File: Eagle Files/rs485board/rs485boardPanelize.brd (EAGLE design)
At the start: 63.5 x 76.7 mm, 95 parts, among them IC1 XC6206P332MR, IC2 MP2562, J1 AVR_SPI_PROG_3X2PTH, J2 RA 6Pin SMD, Q1 CJ3404, Q2 CJ3404, Q3 CJ3404, U1 ATMEGA328P_TQFP, U2 LIS3DH, U3 SP485, X1 RJ45-8P8C-8L-B, X3 RJ45-8P8C-8L-B, Y1 16MHz

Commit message: ready to panelize
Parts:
- added E$1: (no value), misc:MRK_DELTAX
- added E$2: (no value), misc:MRK_DELTAY
- added E$3: (no value), misc:MRK_DOWN_LEFT
- added E$4: 1, misc:NBR_MODX
- added E$5: 2, misc:NBR_MODY
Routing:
- removed copper zone on layer 1, net +5V
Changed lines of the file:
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@@
 <?xml version="1.0" encoding="utf-8"?>
 <!DOCTYPE eagle SYSTEM "eagle.dtd">
-<eagle version="8.7.0">
+<eagle version="9.0.0">
 <drawing>
 <settings>
@@
 <attribute name="VALUE" x="36.56" y="63.114" size="0.8128" layer="27" rot="R180"/>
 </element>
+<element name="E$1" library="misc" package="MRK_DELTAX" value="" x="71.12" y="-2.286"/>
+<element name="E$2" library="misc" package="MRK_DELTAY" value="" x="-6.604" y="76.454"/>
+<element name="E$3" library="misc" package="MRK_DOWN_LEFT" value="" x="-6.35" y="-3.81"/>
+<element name="E$4" library="misc" package="NBR_MODX" value="1" x="26.162" y="-5.08"/>
+<element name="E$5" library="misc" package="NBR_MODY" value="2" x="-21.844" y="42.418"/>
 </elements>
 <signals>
@@
 <contactref element="C38" pad="1"/>
 <contactref element="R9" pad="2"/>
-<polygon width="0.254" layer="1">
-<vertex x="36.068" y="56.642"/>
-<vertex x="37.338" y="56.642"/>
-<vertex x="37.592" y="56.896"/>
-<vertex x="38.354" y="57.658"/>
-<vertex x="38.354" y="72.644"/>
-<vertex x="38.354" y="74.676"/>
-<vertex x="38.1" y="74.93"/>
-<vertex x="36.83" y="74.93"/>
-<vertex x="36.576" y="74.676"/>
-<vertex x="36.068" y="74.168"/>
-</polygon>
-<wire x1="37.465" y1="69.85" x2="37.465" y2="62.119" width="1.27" layer="1"/>
-<wire x1="37.465" y1="62.119" x2="36.56" y2="61.214" width="0.254" layer="1"/>
-<wire x1="36.56" y1="61.214" x2="36.56" y2="57.404" width="0.254" layer="1"/>
+<wire x1="37.465" y1="69.85" x2="37.465" y2="62.119" width="1.524" layer="1"/>
+<wire x1="37.465" y1="62.119" x2="36.56" y2="61.214" width="0.762" layer="1"/>
+<wire x1="36.56" y1="61.214" x2="36.56" y2="57.404" width="0.762" layer="1"/>
 <via x="37.846" y="61.214" extent="1-16" drill="0.35"/>
 <via x="39.37" y="73.406" extent="1-16" drill="0.35"/>
@@
 <via x="9.906" y="69.85" extent="1-16" drill="0.35"/>
 <wire x1="9.906" y1="69.85" x2="9.906" y2="68.006" width="0.254" layer="1"/>
-<wire x1="36.56" y1="61.214" x2="37.846" y2="61.214" width="0.254" layer="1"/>
+<wire x1="36.56" y1="61.214" x2="37.846" y2="61.214" width="0.508" layer="1"/>
 <wire x1="37.846" y1="61.214" x2="38.862" y2="61.214" width="0.254" layer="1"/>
 <wire x1="38.862" y1="61.214" x2="39.37" y2="61.722" width="0.254" layer="1"/>

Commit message: adjust spacing
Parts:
- E$4: value 1 -> 2
- moved E$1 8.01 mm to (63.1, -2.54)
- moved E$2 4.06 mm to (-2.54, 76.5)
- moved E$3 4.02 mm to (-2.54, -2.54)
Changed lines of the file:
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@@
 <attribute name="VALUE" x="36.56" y="63.114" size="0.8128" layer="27" rot="R180"/>
 </element>
-<element name="E$1" library="misc" package="MRK_DELTAX" value="" x="71.12" y="-2.286"/>
-<element name="E$2" library="misc" package="MRK_DELTAY" value="" x="-6.604" y="76.454"/>
-<element name="E$3" library="misc" package="MRK_DOWN_LEFT" value="" x="-6.35" y="-3.81"/>
-<element name="E$4" library="misc" package="NBR_MODX" value="1" x="26.162" y="-5.08"/>
+<element name="E$1" library="misc" package="MRK_DELTAX" value="" x="63.119" y="-2.54"/>
+<element name="E$2" library="misc" package="MRK_DELTAY" value="" x="-2.54" y="76.454"/>
+<element name="E$3" library="misc" package="MRK_DOWN_LEFT" value="" x="-2.54" y="-2.54"/>
+<element name="E$4" library="misc" package="NBR_MODX" value="2" x="26.162" y="-5.08"/>
 <element name="E$5" library="misc" package="NBR_MODY" value="2" x="-21.844" y="42.418"/>
 </elements>

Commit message: clean up 2*2
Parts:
- added C10X12, C10X21, C10X22, C14X12, C14X21, C14X22, C15X12, C15X21, C15X22, C16X12, C16X21, C16X22, C17X12, C17X21, C17X22, C18X12, C18X21, C18X22, C19X12, C19X21, C19X22, C1X12, C1X21, C1X22, C20X12, C20X21, C20X22, C21X12, C21X21, C21X22, C22X12, C22X21, C22X22, C23X12, C23X21, C23X22, C24X12, C24X21, C24X22, C25X12, C25X21, C25X22, C26X12, C26X21, C26X22, C3X12, C3X21, C3X22, C4X12, C4X21, C4X22, C5X12, C5X21, C5X22, C7X12, C7X21, C7X22, C8X12, C8X21, C8X22, C9X12, C9X21, C9X22: 0.1uF, resistor:C0805K
- added C12X12, C12X21, C12X22, C2X12, C2X21, C2X22, C38X12, C38X21, C38X22, C6X12, C6X21, C6X22: 10uF, resistor:C0805K
- added C13X12, C13X21, C13X22, C27X12, C27X21, C27X22, C28X12, C28X21, C28X22, C29X12, C29X21, C29X22, C30X12, C30X21, C30X22, C31X12, C31X21, C31X22, C32X12, C32X21, C32X22, C33X12, C33X21, C33X22, C34X12, C34X21, C34X22, C35X12, C35X21, C35X22: 1uF 100V, SparkFun-Capacitors:1206
- added C36X12, C36X21, C36X22: 150pF, resistor:C0805K
- added D10X12, D10X21, D10X22, D11X12, D11X21, D11X22, D12X12, D12X21, D12X22, D13X12, D13X21, D13X22, D14X12, D14X21, D14X22, D15X12, D15X21, D15X22, D16X12, D16X21, D16X22, D17X12, D17X21, D17X22, D18X12, D18X21, D18X22, D7X12, D7X21, D7X22, D8X12, D8X21, D8X22, D9X12, D9X21, D9X22: WS2812B, SparkFun-LED:WS2812B
- added D1X12, D1X21, D1X22, D2X12, D2X21, D2X22, D3X12, D3X21, D3X22, D4X12, D4X21, D4X22, D5X12, D5X21, D5X22, D6X12, D6X21, D6X22: 5819, adafruit:SOD-123
- added D20X12, D20X21, D20X22: B280-13-F, diode:DO214AA
- added IC1X12, IC1X21, IC1X22: XC6206P332MR, linear:SOT23
- added IC2X12, IC2X21, IC2X22: MP2562, misc:SO08
- added J1X12, J1X21, J1X22: AVR_SPI_PROG_3X2PTH, SparkFun-Connectors:2X3
- added J2X12, J2X21, J2X22: RA 6Pin SMD, SparkFun-Connectors:1X06-SMD_RA_MALE
- added J3X12, J3X21, J3X22, J4X12, J4X21, J4X22, J5X12, J5X21, J5X22, J6X12, J6X21, J6X22: (no value), SparkFun-Connectors:1X01
- added L1X12, L1X21, L1X22: 15uH, misc:SLF12575
- added PAD1X12, PAD1X21, PAD1X22, PAD2X12, PAD2X21, PAD2X22, PAD3X12, PAD3X21, PAD3X22, PAD4X12, PAD4X21, PAD4X22, PAD5X12, PAD5X21, PAD5X22: (no value), wirepad:1,6/0,8
- added Q1X12, Q1X21, Q1X22, Q2X12, Q2X21, Q2X22, Q3X12, Q3X21, Q3X22: CJ3404, SparkFun-DiscreteSemi:SOT23-3
- added R10X12, R10X21, R10X22: 40.2k, resistor:R0805
- added R11X12, R11X21, R11X22: 120, resistor:R0805
- added R12X12, R12X21, R12X22, R13X12, R13X21, R13X22: 1K, resistor:R0805
- added R14X12, R14X21, R14X22, R1X12, R1X21, R1X22, R5X12, R5X21, R5X22, R6X12, R6X21, R6X22, R7X12, R7X21, R7X22: 10K, resistor:R0805
- added R15X12, R15X21, R15X22: 17.4K, resistor:R0805
- added R16X12, R16X21, R16X22: 200K, resistor:R0805
- added R17X12, R17X21, R17X22: 158K, resistor:R0805
- added R2X12, R2X21, R2X22, R3X12, R3X21, R3X22, R4X12, R4X21, R4X22: DNP, resistor:R0805
- added R8X12, R8X21, R8X22: 100K, resistor:R0805
- added R9X12, R9X21, R9X22: 210K, resistor:R0805
- added U1X12, U1X21, U1X22: ATMEGA328P_TQFP, SparkFun-IC-Microcontroller:TQFP32-08
- added U2X12, U2X21, U2X22: LIS3DH, SparkFun-Sensors:LGA-16-3X3
- added U3X12, U3X21, U3X22: SP485, SparkFun-IC-Comms:SO08
- added X1X12, X1X21, X1X22, X3X12, X3X21, X3X22: RJ45-8P8C-8L-B, myownParts:RJ45-SHIELD-DS1128-S80BP
- added Y1X12, Y1X21, Y1X22: 16MHz, SparkFun-Clocks:RESONATOR-SMD-3.2X1.3
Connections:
- new net +24VX12: C13X12.1, C27X12.1, C28X12.1, C29X12.1, C30X12.1, C31X12.1, C32X12.1, C33X12.1, C34X12.1, C35X12.1, IC2X12.7, R8X12.2, X1X12.4, X1X12.5, X3X12.4, X3X12.5
- new net +24VX21: C13X21.1, C27X21.1, C28X21.1, C29X21.1, C30X21.1, C31X21.1, C32X21.1, C33X21.1, C34X21.1, C35X21.1, IC2X21.7, R8X21.2, X1X21.4, X1X21.5, X3X21.4, X3X21.5
- new net +24VX22: C13X22.1, C27X22.1, C28X22.1, C29X22.1, C30X22.1, C31X22.1, C32X22.1, C33X22.1, C34X22.1, C35X22.1, IC2X22.7, R8X22.2, X1X22.4, X1X22.5, X3X22.4, X3X22.5
- new net +3V3X12: C6X12.1, C7X12.1, C9X12.1, IC1X12.2, R5X12.2, R6X12.2, R7X12.2, U2X12.1, U2X12.14
- new net +3V3X21: C6X21.1, C7X21.1, C9X21.1, IC1X21.2, R5X21.2, R6X21.2, R7X21.2, U2X21.1, U2X21.14
- new net +3V3X22: C6X22.1, C7X22.1, C9X22.1, IC1X22.2, R5X22.2, R6X22.2, R7X22.2, U2X22.1, U2X22.14
- new net +5VX12: C12X12.1, C14X12.1, C15X12.1, C16X12.1, C17X12.1, C18X12.1, C19X12.1, C20X12.1, C21X12.1, C22X12.1, C23X12.1, C24X12.1, C25X12.1, C26X12.1, C2X12.1, C38X12.1, C3X12.1, C4X12.1, C8X12.1, D10X12.1, D11X12.1, D12X12.1, D13X12.1, D14X12.1, D15X12.1, D16X12.1, D17X12.1, D18X12.1, D7X12.1, D8X12.1, D9X12.1, IC1X12.3, J1X12.2, J2X12.4, J6X12.1, L1X12.P$2, R14X12.2, R1X12.2, R9X12.2, U1X12.18, U1X12.4, U1X12.6, U3X12.8
- new net +5VX21: C12X21.1, C14X21.1, C15X21.1, C16X21.1, C17X21.1, C18X21.1, C19X21.1, C20X21.1, C21X21.1, C22X21.1, C23X21.1, C24X21.1, C25X21.1, C26X21.1, C2X21.1, C38X21.1, C3X21.1, C4X21.1, C8X21.1, D10X21.1, D11X21.1, D12X21.1, D13X21.1, D14X21.1, D15X21.1, D16X21.1, D17X21.1, D18X21.1, D7X21.1, D8X21.1, D9X21.1, IC1X21.3, J1X21.2, J2X21.4, J6X21.1, L1X21.P$2, R14X21.2, R1X21.2, R9X21.2, U1X21.18, U1X21.4, U1X21.6, U3X21.8
- new net +5VX22: C12X22.1, C14X22.1, C15X22.1, C16X22.1, C17X22.1, C18X22.1, C19X22.1, C20X22.1, C21X22.1, C22X22.1, C23X22.1, C24X22.1, C25X22.1, C26X22.1, C2X22.1, C38X22.1, C3X22.1, C4X22.1, C8X22.1, D10X22.1, D11X22.1, D12X22.1, D13X22.1, D14X22.1, D15X22.1, D16X22.1, D17X22.1, D18X22.1, D7X22.1, D8X22.1, D9X22.1, IC1X22.3, J1X22.2, J2X22.4, J6X22.1, L1X22.P$2, R14X22.2, R1X22.2, R9X22.2, U1X22.18, U1X22.4, U1X22.6, U3X22.8
- new net A3X12: D7X12.4, U1X12.26
- new net A3X21: D7X21.4, U1X21.26
- new net A3X22: D7X22.4, U1X22.26
- new net A4X12: PAD3X12.1, U1X12.27
- new net A4X21: PAD3X21.1, U1X21.27
- new net A4X22: PAD3X22.1, U1X22.27
- new net A5X12: PAD4X12.1, U1X12.28
- new net A5X21: PAD4X21.1, U1X21.28
- new net A5X22: PAD4X22.1, U1X22.28
- new net AREFX12: C5X12.2, U1X12.20
- new net AREFX21: C5X21.2, U1X21.20
- new net AREFX22: C5X22.2, U1X22.20
- new net BSTX12: C10X12.1, IC2X12.8
- new net BSTX21: C10X21.1, IC2X21.8
- new net BSTX22: C10X22.1, IC2X22.8
- new net COMPX12: C36X12.1, IC2X12.3
- new net COMPX21: C36X21.1, IC2X21.3
- new net COMPX22: C36X22.1, IC2X22.3
- new net D2X12: D5X12.C, U1X12.32
- new net D2X21: D5X21.C, U1X21.32
- new net D2X22: D5X22.C, U1X22.32
- new net D3X12: D6X12.C, U1X12.1
- new net D3X21: D6X21.C, U1X21.1
- new net D3X22: D6X22.C, U1X22.1
- new net D5X12: Q3X12.1, U1X12.9
- new net D5X21: Q3X21.1, U1X21.9
- new net D5X22: Q3X22.1, U1X22.9
- new net D6X12: Q2X12.1, U1X12.10
- new net D6X21: Q2X21.1, U1X21.10
- new net D6X22: Q2X22.1, U1X22.10
- new net D7X12: PAD1X12.1, U1X12.11
- new net D7X21: PAD1X21.1, U1X21.11
- new net D7X22: PAD1X22.1, U1X22.11
- new net D8X12: PAD2X12.1, U1X12.12
- new net D8X21: PAD2X21.1, U1X21.12
- new net D8X22: PAD2X22.1, U1X22.12
- new net D9X12: Q1X12.1, U1X12.13
- new net D9X21: Q1X21.1, U1X21.13
- new net D9X22: Q1X22.1, U1X22.13
- new net DIRX12: U1X12.2, U3X12.2, U3X12.3
- new net DIRX21: U1X21.2, U3X21.2, U3X21.3
- new net DIRX22: U1X22.2, U3X22.2, U3X22.3
- new net ENX12: IC2X12.2, R15X12.2, R8X12.1
- new net ENX21: IC2X21.2, R15X21.2, R8X21.1
- new net ENX22: IC2X22.2, R15X22.2, R8X22.1
- new net FBX12: IC2X12.4, R10X12.2, R9X12.1
- new net FBX21: IC2X21.4, R10X21.2, R9X21.1
- new net FBX22: IC2X22.4, R10X22.2, R9X22.1
- new net FREQX12: IC2X12.6, R16X12.2
- new net FREQX21: IC2X21.6, R16X21.2
- new net FREQX22: IC2X22.6, R16X22.2
- new net GNDX12: C12X12.2, C13X12.2, C14X12.2, C15X12.2, C16X12.2, C17X12.2, C18X12.2, C19X12.2, C20X12.2, C21X12.2, C22X12.2, C23X12.2, C24X12.2, C25X12.2, C26X12.2, C27X12.2, C28X12.2, C29X12.2, C2X12.2, C30X12.2, C31X12.2, C32X12.2, C33X12.2, C34X12.2, C35X12.2, C38X12.2, C3X12.2, C4X12.2, C5X12.1, C6X12.2, C7X12.2, C8X12.2, C9X12.2, D10X12.3, D11X12.3, D12X12.3, D13X12.3, D14X12.3, D15X12.3, D16X12.3, D17X12.3, D18X12.3, D20X12.A, D7X12.3, D8X12.3, D9X12.3, IC1X12.1, IC2X12.5, J1X12.6, J2X12.6, PAD5X12.1, Q1X12.2, Q2X12.2, Q3X12.2, R10X12.1, R15X12.1, R16X12.1, R17X12.1, U1X12.21, U1X12.3, U1X12.5, U2X12.10, U2X12.12, U2X12.5, U3X12.5, X1X12.3, X1X12.6, X1X12.7, X1X12.8, X3X12.3, X3X12.6, X3X12.7, X3X12.8, Y1X12.2
- new net GNDX21: C12X21.2, C13X21.2, C14X21.2, C15X21.2, C16X21.2, C17X21.2, C18X21.2, C19X21.2, C20X21.2, C21X21.2, C22X21.2, C23X21.2, C24X21.2, C25X21.2, C26X21.2, C27X21.2, C28X21.2, C29X21.2, C2X21.2, C30X21.2, C31X21.2, C32X21.2, C33X21.2, C34X21.2, C35X21.2, C38X21.2, C3X21.2, C4X21.2, C5X21.1, C6X21.2, C7X21.2, C8X21.2, C9X21.2, D10X21.3, D11X21.3, D12X21.3, D13X21.3, D14X21.3, D15X21.3, D16X21.3, D17X21.3, D18X21.3, D20X21.A, D7X21.3, D8X21.3, D9X21.3, IC1X21.1, IC2X21.5, J1X21.6, J2X21.6, PAD5X21.1, Q1X21.2, Q2X21.2, Q3X21.2, R10X21.1, R15X21.1, R16X21.1, R17X21.1, U1X21.21, U1X21.3, U1X21.5, U2X21.10, U2X21.12, U2X21.5, U3X21.5, X1X21.3, X1X21.6, X1X21.7, X1X21.8, X3X21.3, X3X21.6, X3X21.7, X3X21.8, Y1X21.2
- new net GNDX22: C12X22.2, C13X22.2, C14X22.2, C15X22.2, C16X22.2, C17X22.2, C18X22.2, C19X22.2, C20X22.2, C21X22.2, C22X22.2, C23X22.2, C24X22.2, C25X22.2, C26X22.2, C27X22.2, C28X22.2, C29X22.2, C2X22.2, C30X22.2, C31X22.2, C32X22.2, C33X22.2, C34X22.2, C35X22.2, C38X22.2, C3X22.2, C4X22.2, C5X22.1, C6X22.2, C7X22.2, C8X22.2, C9X22.2, D10X22.3, D11X22.3, D12X22.3, D13X22.3, D14X22.3, D15X22.3, D16X22.3, D17X22.3, D18X22.3, D20X22.A, D7X22.3, D8X22.3, D9X22.3, IC1X22.1, IC2X22.5, J1X22.6, J2X22.6, PAD5X22.1, Q1X22.2, Q2X22.2, Q3X22.2, R10X22.1, R15X22.1, R16X22.1, R17X22.1, U1X22.21, U1X22.3, U1X22.5, U2X22.10, U2X22.12, U2X22.5, U3X22.5, X1X22.3, X1X22.6, X1X22.7, X1X22.8, X3X22.3, X3X22.6, X3X22.7, X3X22.8, Y1X22.2
- new net INT1X12: D5X12.A, U2X12.11
- new net INT1X21: D5X21.A, U2X21.11
- new net INT1X22: D5X22.A, U2X22.11
- new net INT2X12: D6X12.A, U2X12.9
- new net INT2X21: D6X21.A, U2X21.9
- new net INT2X22: D6X22.A, U2X22.9
- new net MISOX12: D3X12.C, J1X12.1, U1X12.16
- new net MISOX21: D3X21.C, J1X21.1, U1X21.16
- new net MISOX22: D3X22.C, J1X22.1, U1X22.16
- new net MISO_3.3VX12: D3X12.A, U2X12.7
- new net MISO_3.3VX21: D3X21.A, U2X21.7
- new net MISO_3.3VX22: D3X22.A, U2X22.7
- new net MOSIX12: D2X12.C, J1X12.4, U1X12.15
- new net MOSIX21: D2X21.C, J1X21.4, U1X21.15
- new net MOSIX22: D2X22.C, J1X22.4, U1X22.15
- new net MOSI_3.3VX12: D2X12.A, R6X12.1, U2X12.6
- new net MOSI_3.3VX21: D2X21.A, R6X21.1, U2X21.6
- new net MOSI_3.3VX22: D2X22.A, R6X22.1, U2X22.6
- new net N$10X12: D10X12.2, D11X12.4
- new net N$10X21: D10X21.2, D11X21.4
- new net N$10X22: D10X22.2, D11X22.4
- new net N$11X12: D11X12.2, D12X12.4
- new net N$11X21: D11X21.2, D12X21.4
- new net N$11X22: D11X22.2, D12X22.4
- new net N$12X12: D12X12.2, D13X12.4
- new net N$12X21: D12X21.2, D13X21.4
- new net N$12X22: D12X22.2, D13X22.4
- new net N$13X12: D13X12.2, D14X12.4
- new net N$13X21: D13X21.2, D14X21.4
- new net N$13X22: D13X22.2, D14X22.4
- new net N$14X12: D14X12.2, D15X12.4
- new net N$14X21: D14X21.2, D15X21.4
- new net N$14X22: D14X22.2, D15X22.4
- new net N$15X12: D15X12.2, D16X12.4
- new net N$15X21: D15X21.2, D16X21.4
- new net N$15X22: D15X22.2, D16X22.4
- new net N$16X12: D16X12.2, D17X12.4
- new net N$16X21: D16X21.2, D17X21.4
- new net N$16X22: D16X22.2, D17X22.4
- new net N$17X12: D17X12.2, D18X12.4
- new net N$17X21: D17X21.2, D18X21.4
- new net N$17X22: D17X22.2, D18X22.4
- new net N$1X12: Q1X12.3, R2X12.1
- new net N$1X21: Q1X21.3, R2X21.1
- new net N$1X22: Q1X22.3, R2X22.1
- new net N$25X12: C36X12.2, R17X12.2
- new net N$25X21: C36X21.2, R17X21.2
- new net N$25X22: C36X22.2, R17X22.2
- new net N$2X12: D7X12.2, D8X12.4
- new net N$2X21: D7X21.2, D8X21.4
- new net N$2X22: D7X22.2, D8X22.4
- new net N$30X12: R12X12.2, U3X12.1
- new net N$30X21: R12X21.2, U3X21.1
- new net N$30X22: R12X22.2, U3X22.1
- new net N$31X12: R13X12.2, U3X12.4
- new net N$31X21: R13X21.2, U3X21.4
- new net N$31X22: R13X22.2, U3X22.4
- new net N$3X12: D8X12.2, D9X12.4
- new net N$3X21: D8X21.2, D9X21.4
- new net N$3X22: D8X22.2, D9X22.4
- new net N$4X12: J3X12.1, R2X12.2
- new net N$4X21: J3X21.1, R2X21.2
- new net N$4X22: J3X22.1, R2X22.2
- new net N$5X12: Q2X12.3, R3X12.1
- new net N$5X21: Q2X21.3, R3X21.1
- new net N$5X22: Q2X22.3, R3X22.1
- new net N$6X12: J4X12.1, R3X12.2
- new net N$6X21: J4X21.1, R3X21.2
- new net N$6X22: J4X22.1, R3X22.2
- new net N$7X12: Q3X12.3, R4X12.1
- new net N$7X21: Q3X21.3, R4X21.1
- new net N$7X22: Q3X22.3, R4X22.1
- new net N$8X12: J5X12.1, R4X12.2
- new net N$8X21: J5X21.1, R4X21.2
- new net N$8X22: J5X22.1, R4X22.2
- new net N$9X12: D10X12.4, D9X12.2
- new net N$9X21: D10X21.4, D9X21.2
- new net N$9X22: D10X22.4, D9X22.2
- new net RESETX12: C1X12.2, J1X12.5, R1X12.1, U1X12.29
- new net RESETX21: C1X21.2, J1X21.5, R1X21.1, U1X21.29
- new net RESETX22: C1X22.2, J1X22.5, R1X22.1, U1X22.29
- new net RESET_EXTX12: C1X12.1, J2X12.1
- new net RESET_EXTX21: C1X21.1, J2X21.1
- new net RESET_EXTX22: C1X22.1, J2X22.1
- new net RS485AX12: R11X12.1, U3X12.6, X1X12.2, X3X12.2
- new net RS485AX21: R11X21.1, U3X21.6, X1X21.2, X3X21.2
- new net RS485AX22: R11X22.1, U3X22.6, X1X22.2, X3X22.2
- new net RS485BX12: R11X12.2, U3X12.7, X1X12.1, X3X12.1
- new net RS485BX21: R11X21.2, U3X21.7, X1X21.1, X3X21.1
- new net RS485BX22: R11X22.2, U3X22.7, X1X22.1, X3X22.1
- new net RXX12: J2X12.3, R12X12.1, R14X12.1, U1X12.30
- new net RXX21: J2X21.3, R12X21.1, R14X21.1, U1X21.30
- new net RXX22: J2X22.3, R12X22.1, R14X22.1, U1X22.30
- new net SCKX12: D4X12.C, J1X12.3, U1X12.17
- new net SCKX21: D4X21.C, J1X21.3, U1X21.17
- new net SCKX22: D4X22.C, J1X22.3, U1X22.17
- new net SCK_3.3VX12: D4X12.A, R7X12.1, U2X12.4
- new net SCK_3.3VX21: D4X21.A, R7X21.1, U2X21.4
- new net SCK_3.3VX22: D4X22.A, R7X22.1, U2X22.4
- new net SSX12: D1X12.C, U1X12.14
- new net SSX21: D1X21.C, U1X21.14
- new net SSX22: D1X22.C, U1X22.14
- new net SS_3.3VX12: D1X12.A, R5X12.1, U2X12.8
- new net SS_3.3VX21: D1X21.A, R5X21.1, U2X21.8
- new net SS_3.3VX22: D1X22.A, R5X22.1, U2X22.8
- new net SWX12: C10X12.2, D20X12.C, IC2X12.1, L1X12.P$1
- new net SWX21: C10X21.2, D20X21.C, IC2X21.1, L1X21.P$1
- new net SWX22: C10X22.2, D20X22.C, IC2X22.1, L1X22.P$1
- new net TXX12: J2X12.2, R13X12.1, U1X12.31
- new net TXX21: J2X21.2, R13X21.1, U1X21.31
- new net TXX22: J2X22.2, R13X22.1, U1X22.31
- new net XTAL1X12: U1X12.7, Y1X12.1
- new net XTAL1X21: U1X21.7, Y1X21.1
- new net XTAL1X22: U1X22.7, Y1X22.1
- new net XTAL2X12: U1X12.8, Y1X12.3
- new net XTAL2X21: U1X21.8, Y1X21.3
- new net XTAL2X22: U1X22.8, Y1X22.3
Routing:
- net GNDX22: track 0.00 -> 654.9 mm, vias 0 -> 70
- net GNDX21: track 0.00 -> 654.9 mm, vias 0 -> 70
- net GNDX12: track 0.00 -> 654.9 mm, vias 0 -> 70
- net +5VX21: track 0.00 -> 417.0 mm, vias 0 -> 14
- net +5VX22: track 0.00 -> 417.0 mm, vias 0 -> 14
- net +5VX12: track 0.00 -> 417.0 mm, vias 0 -> 14
- net +24VX22: track 0.00 -> 119.4 mm, vias 0 -> 2
- net +24VX12: track 0.00 -> 119.4 mm, vias 0 -> 2
- net +24VX21: track 0.00 -> 119.4 mm, vias 0 -> 2
- net RS485AX21: track 0.00 -> 88.7 mm
- net RS485AX22: track 0.00 -> 88.7 mm
- net RS485AX12: track 0.00 -> 88.7 mm
- net TXX22: track 0.00 -> 75.9 mm, vias 0 -> 2
- net TXX21: track 0.00 -> 75.9 mm, vias 0 -> 2
- net TXX12: track 0.00 -> 75.9 mm, vias 0 -> 2
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- added copper zone on layer 1, net GNDX12
- added copper zone on layer 16, net GNDX12
- added copper zone on layer 1, net GNDX21
- added copper zone on layer 16, net GNDX21
- added copper zone on layer 1, net GNDX22
- added copper zone on layer 16, net GNDX22
- added copper zone on layer 1, net SWX12
- added copper zone on layer 1, net SWX21
- added copper zone on layer 1, net SWX22
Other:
- board size 63.5 x 76.7 mm -> 129.2 x 155.6 mm
- board text added: "C14"
- board text added: "C15"
- board text added: "C16"
- board text added: "C17"
- board text added: "C18"
- board text added: "C19"
- board text added: "C20"
- board text added: "C21"
- board text added: "C22"
- board text added: "C23"
- board text added: "C24"
- board text added: "C25"
- board text added: "C32"
- board text added: "D10"
- board text added: "D11"
- board text added: "D12"
- board text added: "D13"
- board text added: "D14"
- board text added: "D15"
- board text added: "D16"
- board text added: "D17"
- board text added: "D18"
- board text added: "D7"
- board text added: "D8"
- board text added: "D9"
- board text added: "J2"
- board text added: "Think Create LLC'"

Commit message: move to AB 2*2
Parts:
- removed E$1: (no value), misc:MRK_DELTAX
- removed E$2: (no value), misc:MRK_DELTAY
- removed E$3: (no value), misc:MRK_DOWN_LEFT
- removed E$4: 2, misc:NBR_MODX
- removed E$5: 2, misc:NBR_MODY
- moved PAD1 141.0 mm to (127.6, 70.0), turned to 180 degrees
- moved PAD2 139.5 mm to (126.1, 71.2), turned to 180 degrees
- moved Y1 135.1 mm to (126.6, 65.2), turned to 90 degrees
- moved C3 130.6 mm to (125.6, 61.6), turned to 0 degrees
- moved C4 129.0 mm to (125.6, 59.3), turned to 0 degrees
- moved D4 128.4 mm to (127.1, 53.0), turned to 270 degrees
- moved R16 127.1 mm to (122.3, 11.8), turned to 270 degrees
- moved R7 126.4 mm to (127.1, 47.6), turned to 270 degrees
- moved J2X21 126.1 mm to (8.89, 67.9), turned to 270 degrees
- moved C32X21 124.6 mm to (9.40, 9.53), turned to 0 degrees
- moved D2 124.5 mm to (125.1, 53.0), turned to 270 degrees
- moved R13X21 124.2 mm to (3.81, 51.2), turned to 270 degrees
- moved R9 123.4 mm to (119.3, 9.78), turned to 270 degrees
- moved U1 122.6 mm to (119.0, 66.7), turned to 135 degrees
- moved C8 122.3 mm to (125.6, 42.5), turned to 90 degrees
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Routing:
- net D6: track 43.1 -> 42.1 mm
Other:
- board size 129.2 x 155.6 mm -> 129.2 x 155.5 mm

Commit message: panel finish, need add fiducial
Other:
- board size 129.2 x 155.5 mm -> 139.6 x 155.8 mm

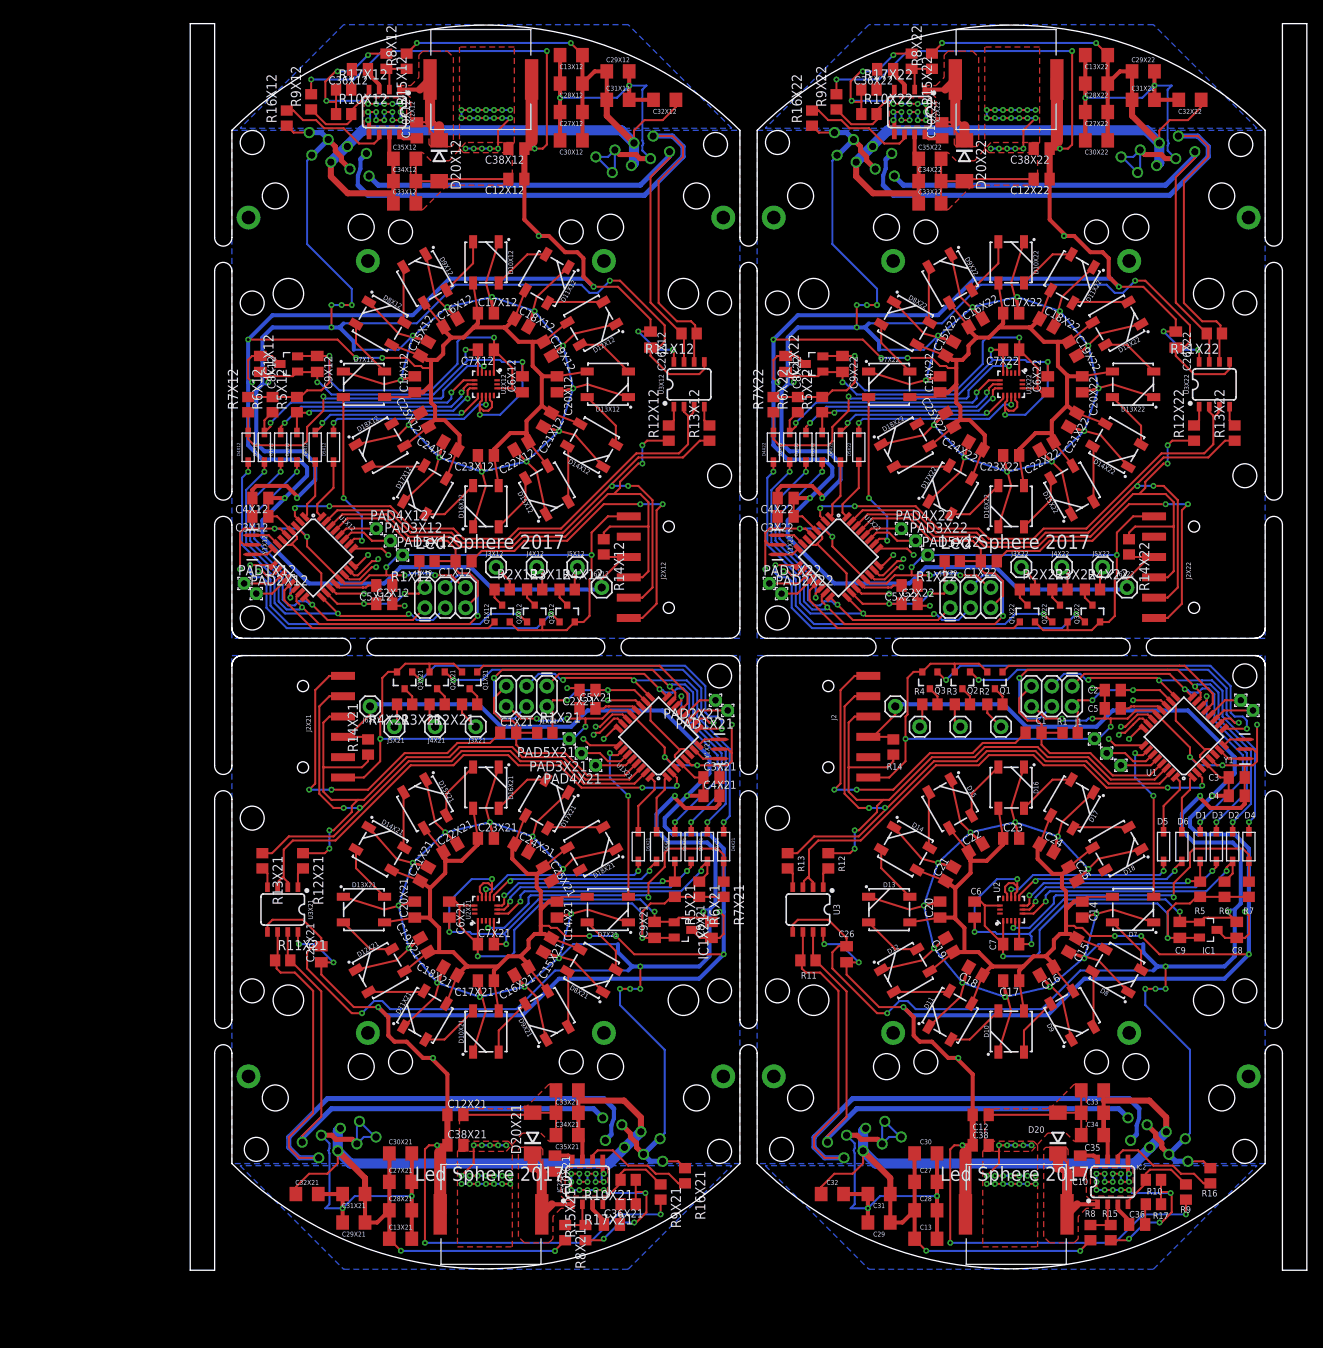
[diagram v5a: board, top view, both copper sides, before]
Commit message: add fiducial
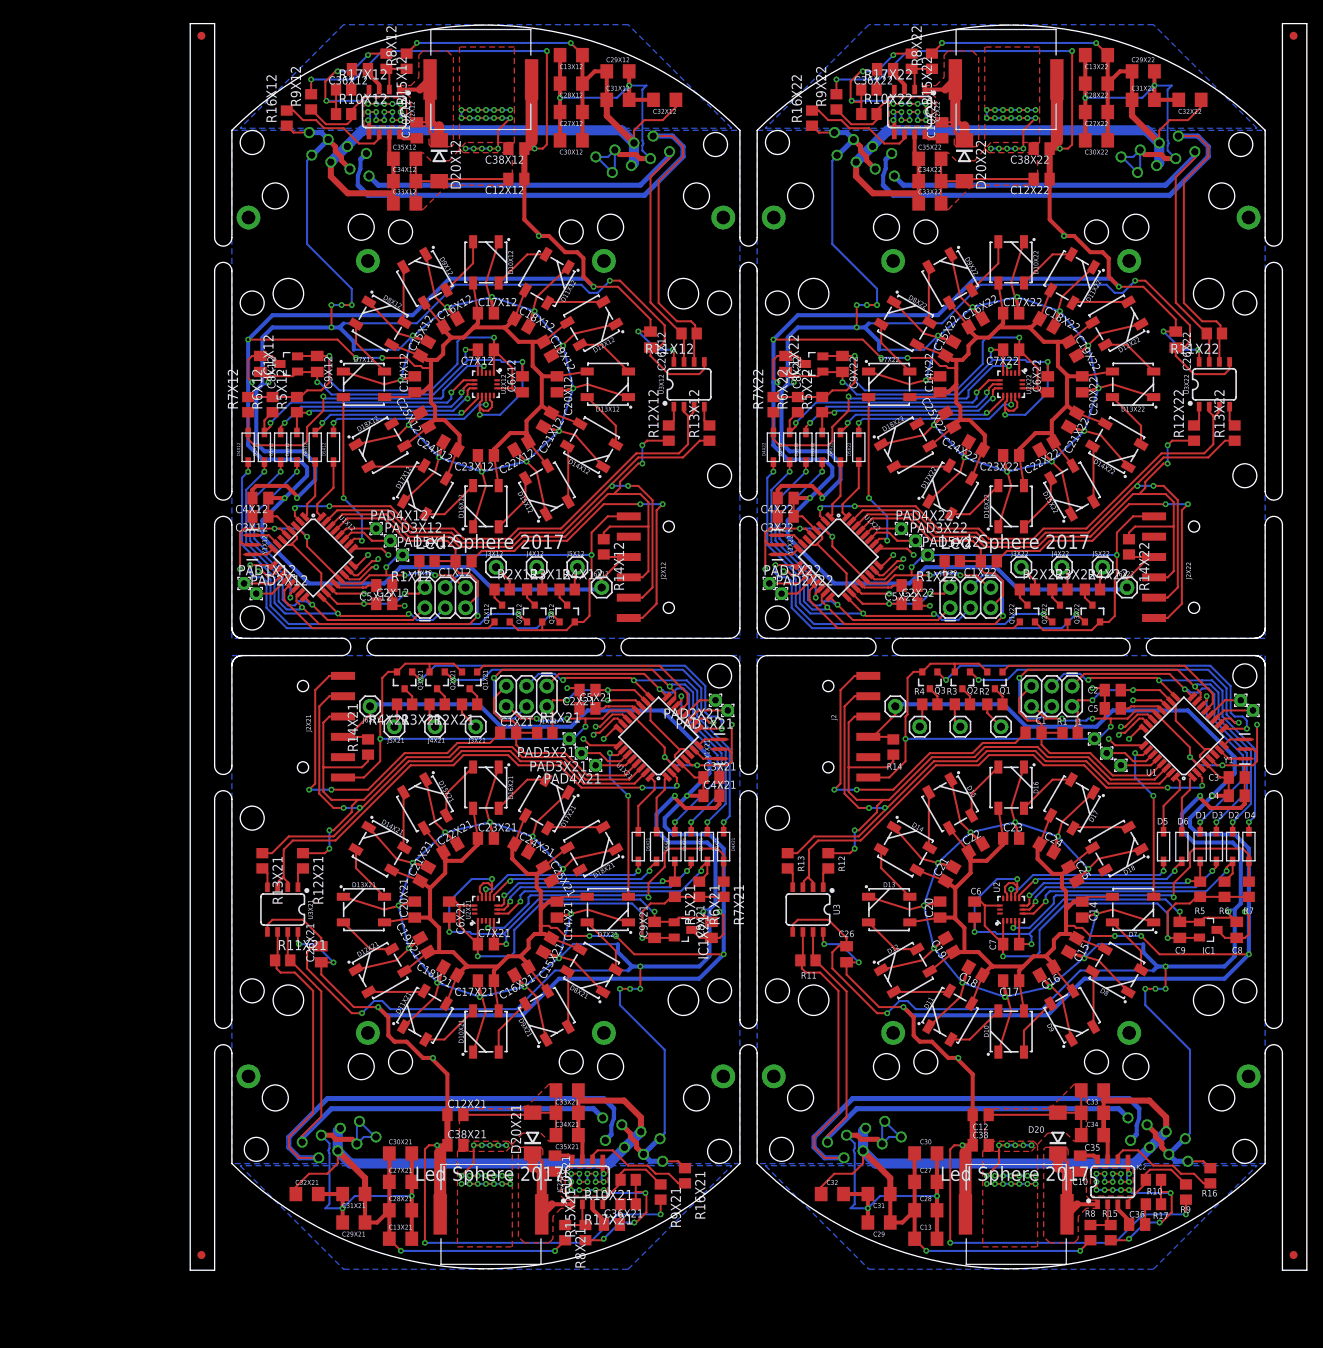
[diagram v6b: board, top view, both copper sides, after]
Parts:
- added E$1, E$2, E$3, E$4: (no value), SparkFun-Aesthetics:FIDUCIAL-1X2
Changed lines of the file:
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@@
 <element name="X3X22" library="myownParts" package="RJ45-SHIELD-DS1128-S80BP" value="RJ45-8P8C-8L-B" x="76.454" y="132.334" rot="MR20"/>
 <element name="Y1X22" library="SparkFun-Clocks" library_urn="urn:adsk.eagle:library:511" package="RESONATOR-SMD-3.2X1.3" package3d_urn="urn:adsk.eagle:package:37551/1" value="16MHz" x="68.199" y="90.678" rot="R270"/>
+<element name="E$1" library="SparkFun-Aesthetics" library_urn="urn:adsk.eagle:library:507" package="FIDUCIAL-1X2" package3d_urn="urn:adsk.eagle:package:37108/1" value="" x="-3.81" y="154.305"/>
+<element name="E$2" library="SparkFun-Aesthetics" library_urn="urn:adsk.eagle:library:507" package="FIDUCIAL-1X2" package3d_urn="urn:adsk.eagle:package:37108/1" value="" x="-3.81" y="1.905"/>
+<element name="E$3" library="SparkFun-Aesthetics" library_urn="urn:adsk.eagle:library:507" package="FIDUCIAL-1X2" package3d_urn="urn:adsk.eagle:package:37108/1" value="" x="132.715" y="1.905"/>
+<element name="E$4" library="SparkFun-Aesthetics" library_urn="urn:adsk.eagle:library:507" package="FIDUCIAL-1X2" package3d_urn="urn:adsk.eagle:package:37108/1" value="" x="132.715" y="154.305"/>
 </elements>
 <signals>
